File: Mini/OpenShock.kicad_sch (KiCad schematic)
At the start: 41 parts, among them J1 USB_C_Receptacle_USB2.0, J2 Conn_01x03, J3 Conn_01x03, J4 Conn_01x06, J6 Conn_01x04, SW1 KH-6X6X6H-TJ, SW2 KH-6X6X6H-TJ, SW3 KH-6X6X6H-TJ, U1 ESP32-S3-WROOM-1, U2 AMS1117-3.3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

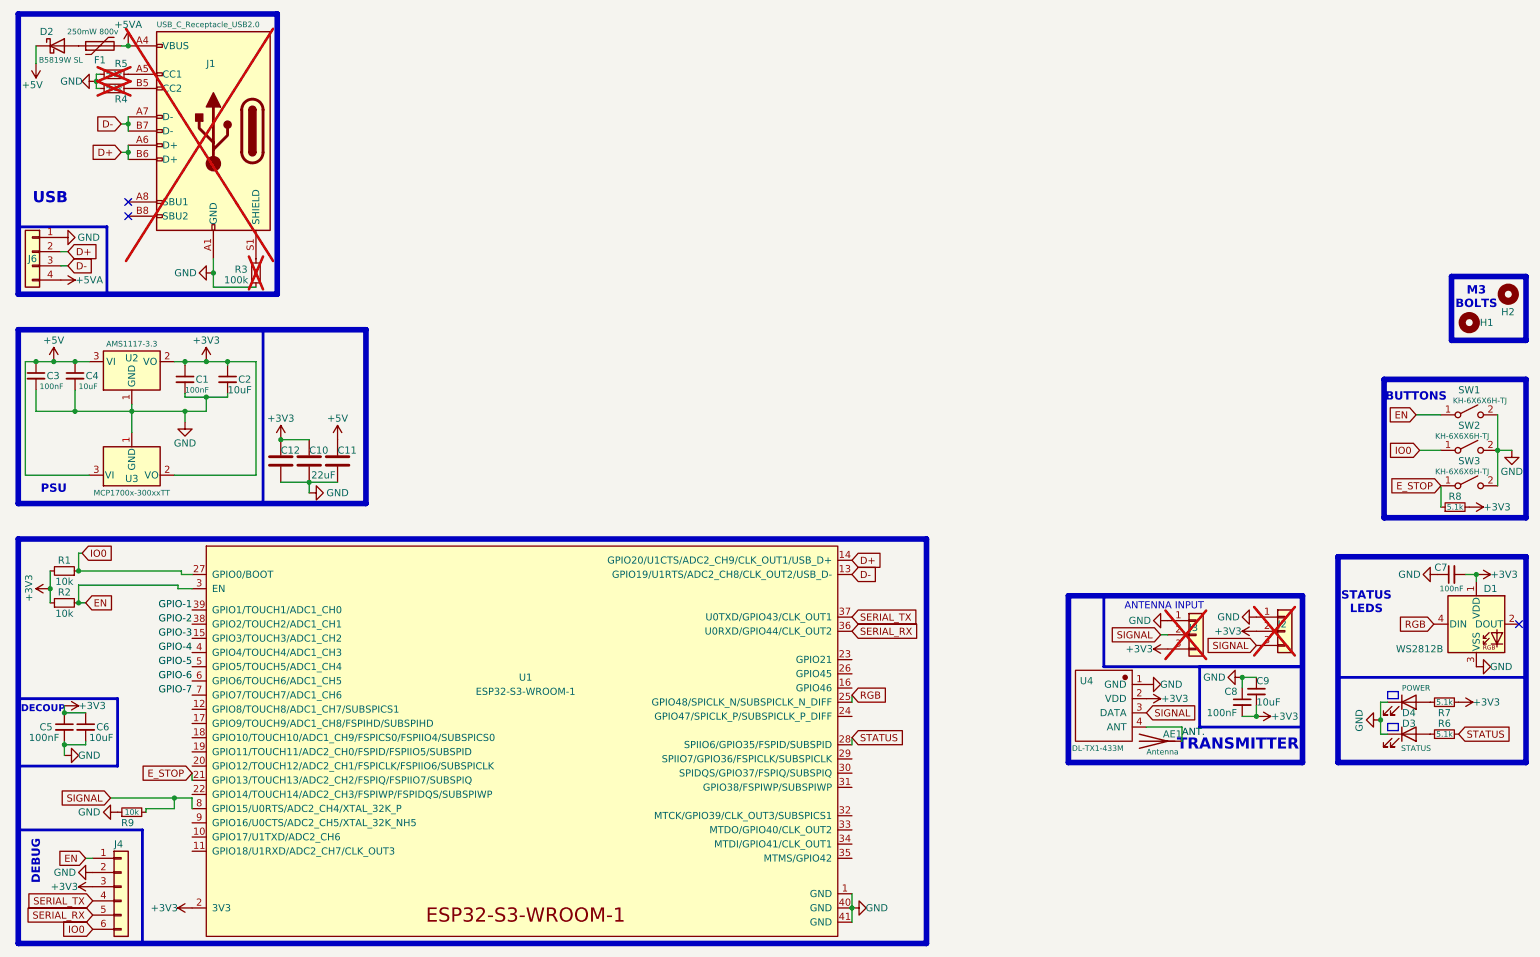
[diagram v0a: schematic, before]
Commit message: Schematic Fixes & Add Title Blocks
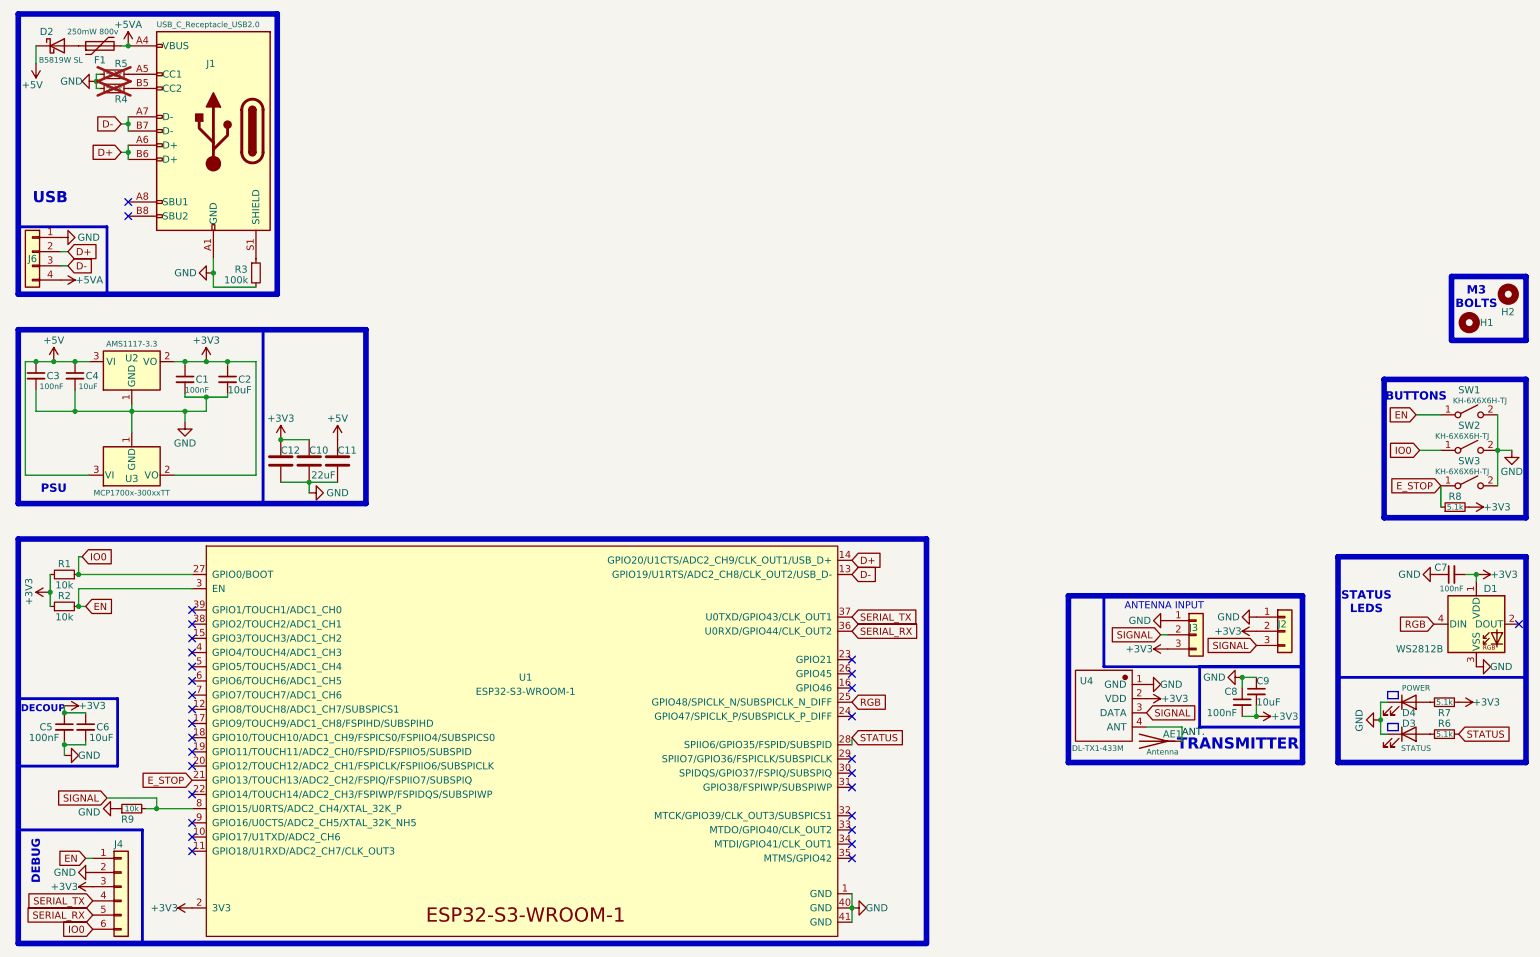
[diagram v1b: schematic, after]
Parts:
- J1, J2, J3, R3: now fitted
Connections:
- net GPIO-1: no longer names the net of U1.39 (GPIO1/TOUCH1/ADC1_CH0)
- net GPIO-2: no longer names the net of U1.38 (GPIO2/TOUCH2/ADC1_CH1)
- net GPIO-3: no longer names the net of U1.15 (GPIO3/TOUCH3/ADC1_CH2)
- net GPIO-4: no longer names the net of U1.4 (GPIO4/TOUCH4/ADC1_CH3)
- net GPIO-5: no longer names the net of U1.5 (GPIO5/TOUCH5/ADC1_CH4)
- net GPIO-6: no longer names the net of U1.6 (GPIO6/TOUCH6/ADC1_CH5)
- net GPIO-7: no longer names the net of U1.7 (GPIO7/TOUCH7/ADC1_CH6)
- no-connect marks 3 -> 30
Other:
- company: (none) -> Pera @ https://transfur.science/f191
- title: (none) -> Open Shock Mini
- moved on the sheet: R1, R2, R9
